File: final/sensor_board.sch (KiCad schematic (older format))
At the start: 77 parts, among them J1 USB_microB_2040002-1, J2 Arduino_ICSP, J3 Conn_01x02_Male, J4 Conn_01x15_Male, J5 Conn_01x15_Male, J6 BT CONFIG, SW1 SW_DIP_x01, U1 NC7SZ04P5X, U10 BQ24075, U11 BQ27441-G1, U2 MCP1702T-3302E/CBCT-ND, U3 TXS0104E, U4 TPS61200DRC, U5 FT232RL, U6 RN4871, U7 TPS2113ADRBR, U8 US5881, U9 ATMEGA328PB-ANR, Y1 16MHz

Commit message: Assign new footprint to capacitor
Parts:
- C23: footprint Capacitor_SMD:C_0603_1608Metric -> Capacitor_SMD:C_0402_1005Metric
- J3: footprint Connector_PinHeader_2.54mm:PinHeader_1x02_P2.54mm_Vertical -> Connector_PinHeader_2.54mm:PinHeader_1x02_P2.54mm_Vertical_SMD_Pin1Right
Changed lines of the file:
@@
 F 0 "J3" H 16823 4280 50  0000 R CNN
 F 1 "Conn_01x02_Male" H 16823 4371 50  0000 R CNN
-F 2 "Connector_PinHeader_2.54mm:PinHeader_1x02_P2.54mm_Vertical" H 16850 4400 50  0001 C CNN
+F 2 "Connector_PinHeader_2.54mm:PinHeader_1x02_P2.54mm_Vertical_SMD_Pin1Right" H 16850 4400 50  0001 C CNN
 F 3 "~" H 16850 4400 50  0001 C CNN
 	1    16850 4400
@@
 F 0 "C23" H 17315 2646 50  0000 L CNN
 F 1 "0.47µF" H 17315 2555 50  0000 L CNN
-F 2 "Capacitor_SMD:C_0603_1608Metric" H 17238 2450 50  0001 C CNN
+F 2 "Capacitor_SMD:C_0402_1005Metric" H 17238 2450 50  0001 C CNN
 F 3 "~" H 17200 2600 50  0001 C CNN
 	1    17200 2600

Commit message: made footprint
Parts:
- J6: footprint (none) -> Connector_PinHeader_2.54mm:PinHeader_1x08_P2.54mm_Vertical
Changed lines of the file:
@@
 EESchema Schematic File Version 4
 LIBS:sensor_board-cache
-EELAYER 26 0
+EELAYER 29 0
 EELAYER END
 $Descr User 18504 11811
@@
 F 0 "J6" H 16843 9283 50  0000 R CNN
 F 1 "BT CONFIG" H 16843 9192 50  0000 R CNN
-F 2 "" H 16870 9310 50  0001 C CNN
+F 2 "Connector_PinHeader_2.54mm:PinHeader_1x08_P2.54mm_Vertical" H 16870 9310 50  0001 C CNN
 F 3 "~" H 16870 9310 50  0001 C CNN
 	1    16870 9310

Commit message: added new footprints and assignments
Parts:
- U1: footprint (none) -> mp3b:NC7SZ04P5X
- U10: footprint (none) -> mp3b:BQ24075
- U4: footprint Package_SON:Texas_S-PVSON-N10_ThermalVias -> mp3b:TPS61200DRC
- U7: footprint (none) -> mp3b:TPS2113ADRBR
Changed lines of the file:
@@
 F 0 "U7" H 8150 3037 60  0000 C CNN
 F 1 "TPS2113ADRBR" H 8150 2931 60  0000 C CNN
-F 2 "" H 8150 2600 60  0001 C CNN
+F 2 "mp3b:TPS2113ADRBR" H 8150 2600 60  0001 C CNN
 F 3 "" H 8150 2600 60  0001 C CNN
 	1    8150 2450
@@
 F 0 "U10" H 12100 3278 50  0000 C CNN
 F 1 "BQ24075" H 12100 3187 50  0000 C CNN
-F 2 "" H 12350 1950 50  0001 L CNN
+F 2 "mp3b:BQ24075" H 12350 1950 50  0001 L CNN
 F 3 "http://www.ti.com/lit/ds/symlink/bq24075.pdf" H 12300 2700 50  0001 C CNN
 	1    12100 2500
@@
 F 0 "U1" H 2150 9535 50  0000 C CNN
 F 1 "NC7SZ04P5X" H 2150 9444 50  0000 C CNN
-F 2 "" H 2150 9210 50  0001 C CNN
+F 2 "mp3b:NC7SZ04P5X" H 2150 9210 50  0001 C CNN
 F 3 "" H 2150 9210 50  0001 C CNN
 	1    2150 9210
@@
 F 0 "U4" H 4750 2767 50  0000 C CNN
 F 1 "TPS61200DRC" H 4750 2676 50  0000 C CNN
-F 2 "Package_SON:Texas_S-PVSON-N10_ThermalVias" H 4750 1850 50  0001 C CNN
+F 2 "mp3b:TPS61200DRC" H 4750 1850 50  0001 C CNN
 F 3 "http://www.ti.com/lit/ds/symlink/tps61200.pdf" H 4750 2300 50  0001 C CNN
 	1    4750 2300

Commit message: Add assignment for small logic converter
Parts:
- U3: footprint (none) -> mp3b:txs0104e
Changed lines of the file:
@@
 EESchema Schematic File Version 4
 LIBS:sensor_board-cache
-EELAYER 29 0
+EELAYER 26 0
 EELAYER END
 $Descr User 18504 11811
@@
 F 0 "U3" H 3505 9034 50  0000 C CNN
 F 1 "TXS0104E" H 3505 8943 50  0000 C CNN
-F 2 "" H 3730 9670 50  0001 C CNN
+F 2 "mp3b:txs0104e" H 3730 9670 50  0001 C CNN
 F 3 "" H 3730 9670 50  0001 C CNN
 	1    3530 9670

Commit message: Final Footprints
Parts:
- D1: footprint (none) -> LED_SMD:LED_0805_2012Metric
- J3: footprint Connector_PinHeader_2.54mm:PinHeader_1x02_P2.54mm_Vertical_SMD_Pin1Right -> mp3b:JST-2-SMD
- L1: footprint (none) -> mp3b:CDRH2D18HP
- SW1: footprint (none) -> mp3b:KAE01SGGt
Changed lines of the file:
@@
 F 0 "D1" H 6491 10056 50  0000 C CNN
 F 1 "BTPWR" H 6491 9965 50  0000 C CNN
-F 2 "" H 6500 9840 50  0001 C CNN
+F 2 "LED_SMD:LED_0805_2012Metric" H 6500 9840 50  0001 C CNN
 F 3 "~" H 6500 9840 50  0001 C CNN
 	1    6500 9840
@@
 F 0 "J3" H 16823 4280 50  0000 R CNN
 F 1 "Conn_01x02_Male" H 16823 4371 50  0000 R CNN
-F 2 "Connector_PinHeader_2.54mm:PinHeader_1x02_P2.54mm_Vertical_SMD_Pin1Right" H 16850 4400 50  0001 C CNN
+F 2 "mp3b:JST-2-SMD" H 16850 4400 50  0001 C CNN
 F 3 "~" H 16850 4400 50  0001 C CNN
 	1    16850 4400
@@
 F 0 "SW1" H 1600 1267 50  0000 C CNN
 F 1 "SW_DIP_x01" H 1600 1176 50  0000 C CNN
-F 2 "" H 1600 1000 50  0001 C CNN
+F 2 "mp3b:KAE01SGGt" H 1600 1000 50  0001 C CNN
 F 3 "" H 1600 1000 50  0001 C CNN
 	1    1600 1000
@@
 F 0 "L1" H 4650 1915 50  0000 C CNN
 F 1 "4.7uH" H 4650 1824 50  0000 C CNN
-F 2 "" H 4650 1700 50  0001 C CNN
+F 2 "mp3b:CDRH2D18HP" H 4650 1700 50  0001 C CNN
 F 3 "http://products.sumida.com/products/pdf/CDRH2D18HP.pdf" H 4650 1700 50  0001 C CNN
 	1    4650 1700

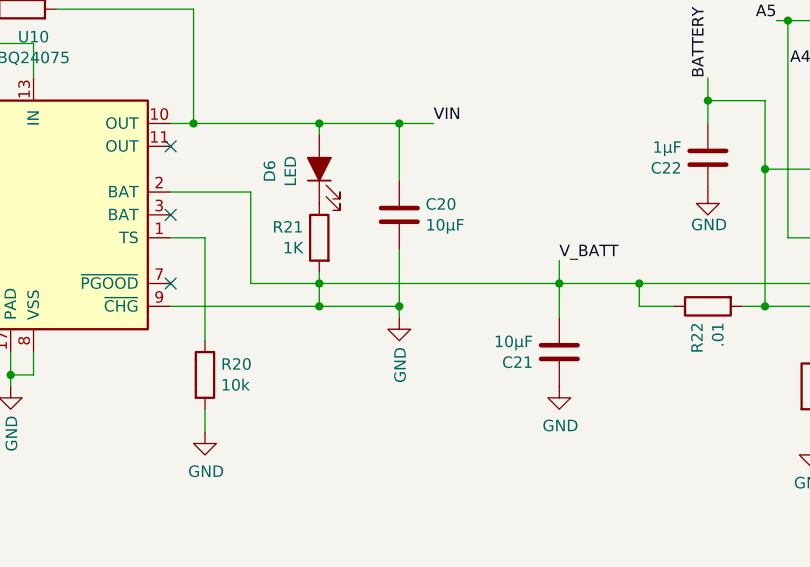
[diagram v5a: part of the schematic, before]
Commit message: Fixed bad junction
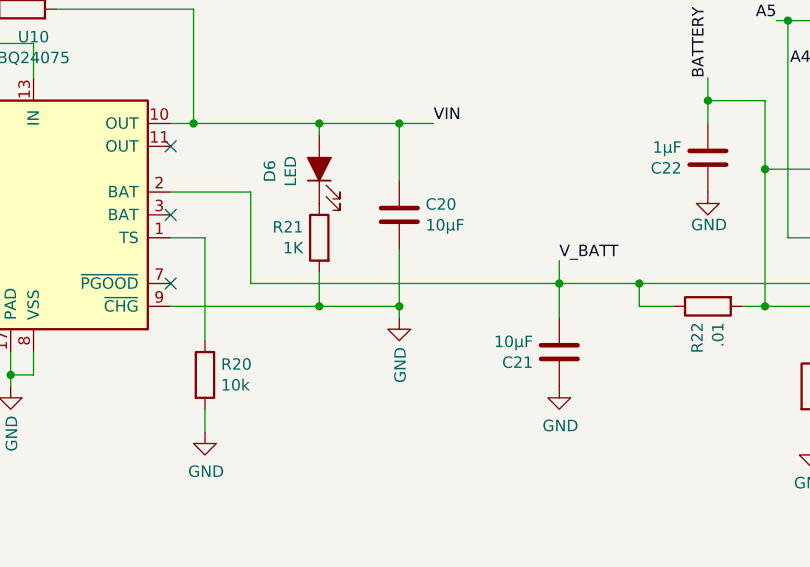
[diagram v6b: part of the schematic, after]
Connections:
- net GND: no longer C21.2, R22.1, U10.2 (BAT), U11.7 (SRN)
- new net V_BATT: C21.2, R22.1, U10.2 (BAT), U11.7 (SRN)
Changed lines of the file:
@@
 Connection ~ 14400 2800
-Wire Wire Line
-	13050 2800 13350 2800
 Wire Wire Line
 	14400 2800 14750 2800
@@
 	13350 2100 13700 2100
 Wire Wire Line
-	13350 2800 14400 2800
-Wire Wire Line
 	13350 2750 13350 2800
 $Comp
@@
 Wire Wire Line
 	1640 9540 1640 9510
-Connection ~ 13350 2800
 Wire Wire Line
 	13350 2800 13350 2900
@@
 Wire Wire Line
 	5250 2300 5150 2300
+Wire Wire Line
+	13050 2800 14400 2800
 $EndSCHEMATC
